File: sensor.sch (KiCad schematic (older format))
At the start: 67 parts, among them CON1 Micro USB, CON2 PROG, CON3 N.C., CON4 HTU21D, CON5 PMS3003/5003, CON6 AUX, Q1 BSS214N, Q2 BSS214N, Q3 BSS214N, SW1 RESET, SW2 CFG, U1 N.C., U2 TLV1117LV33DCY, U3 ESP-12F, U4 HTU21D, U5 PMS7003

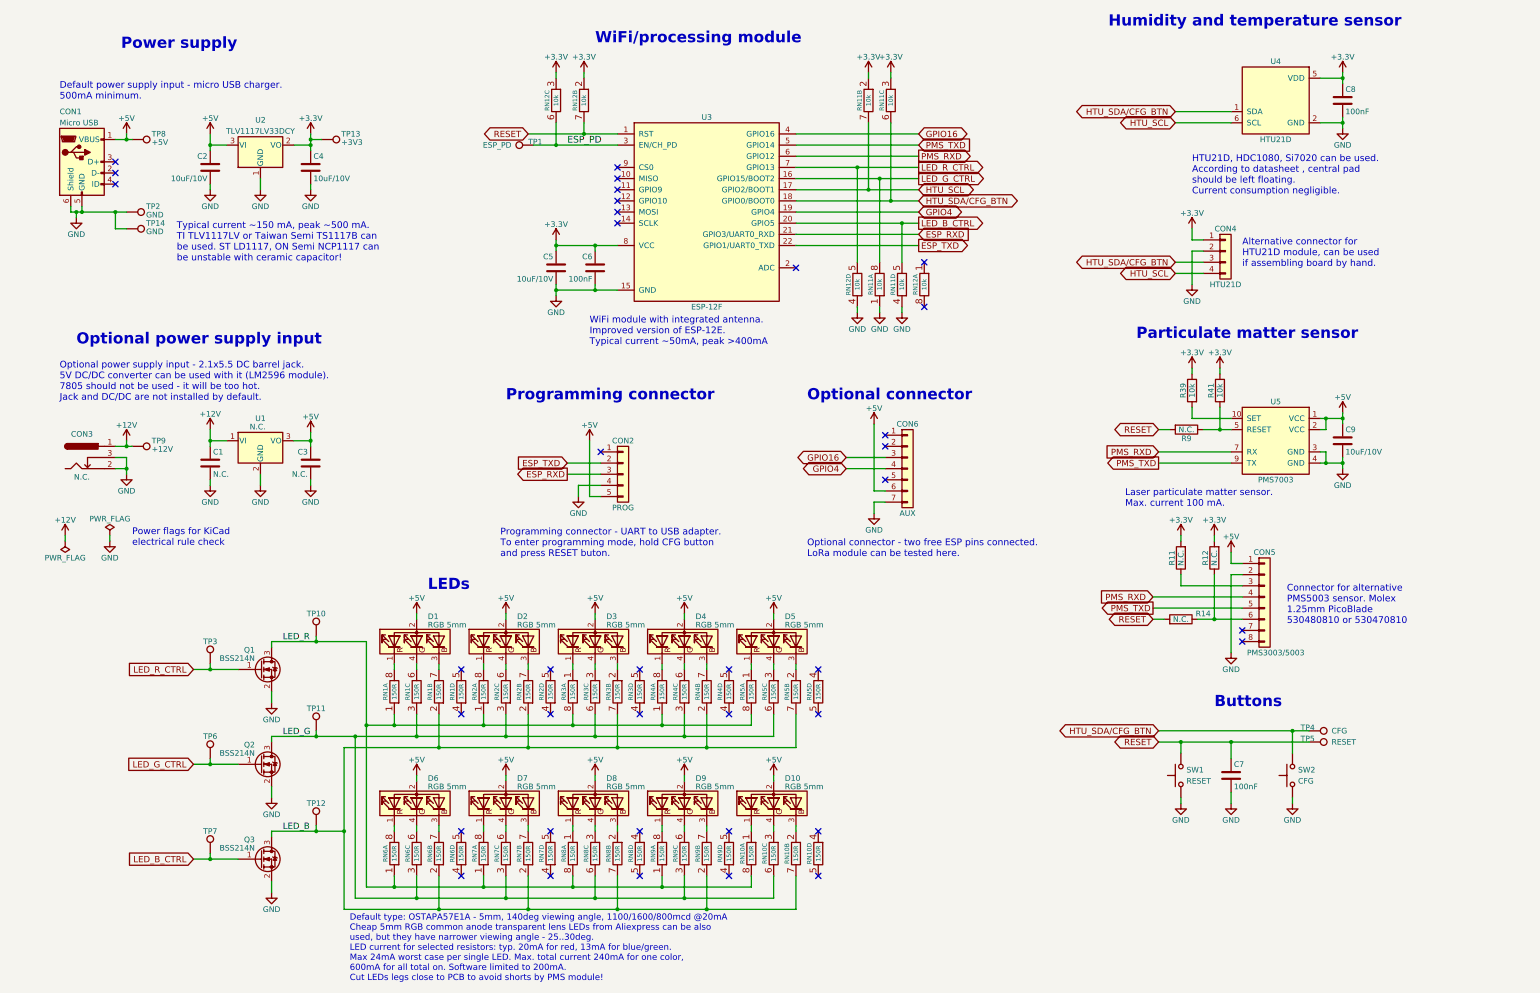
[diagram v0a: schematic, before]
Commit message: Add connector for SDS011 Close #10
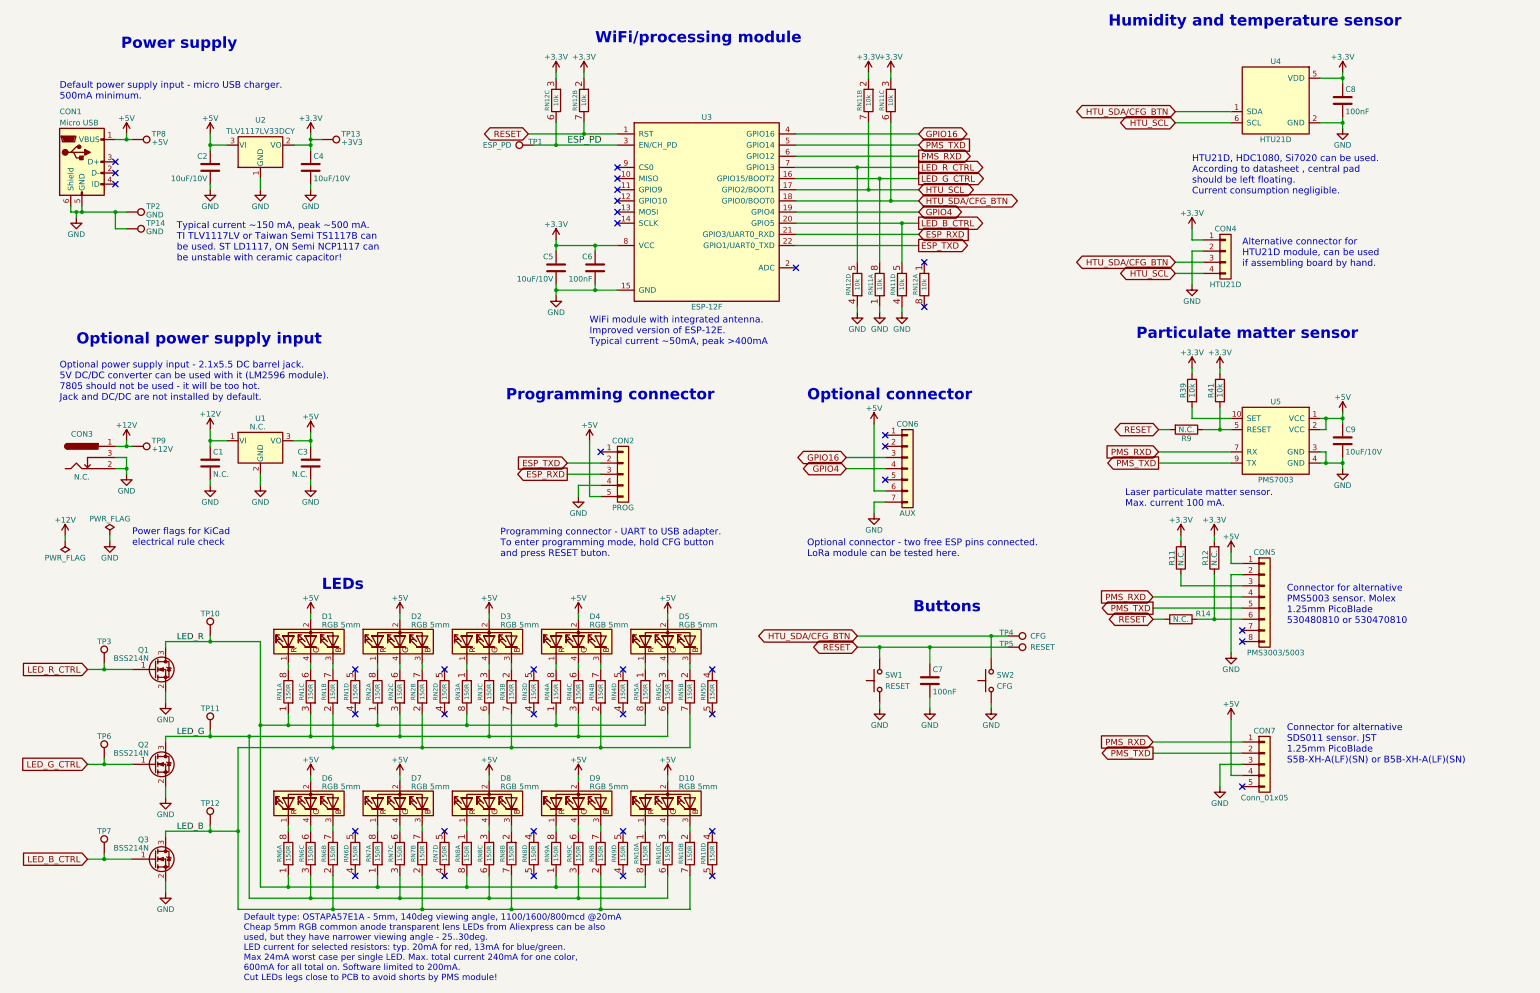
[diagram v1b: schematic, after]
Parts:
- added CON7: Conn_01x05, less-smog:B5B-XH-A(LF)(SN), symbol Conn_01x05
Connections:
- net +5V: now also CON7.4 (Pin_4)
- net GND: now also CON7.3 (Pin_3)
- net PMS_RXD: now also CON7.1 (Pin_1)
- net PMS_TXD: now also CON7.2 (Pin_2)
- no-connect marks 38 -> 39
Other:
- note added: "Connector for alternative\nSDS011 sensor. JST\n1.25mm PicoBlade\nS5B-XH-A(LF)(SN) or B5B-XH-A(LF)(SN)"
- moved on the sheet: C7, D1, D10, D2, D3, D4, D5, D6, D7, D8, D9, Q1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

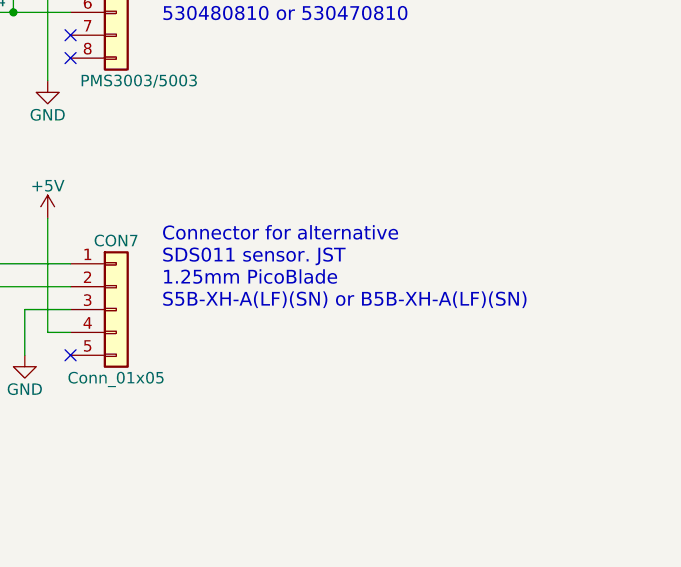
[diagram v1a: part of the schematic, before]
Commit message: [#10] Update schematic PDF. Add remaining library footprints.
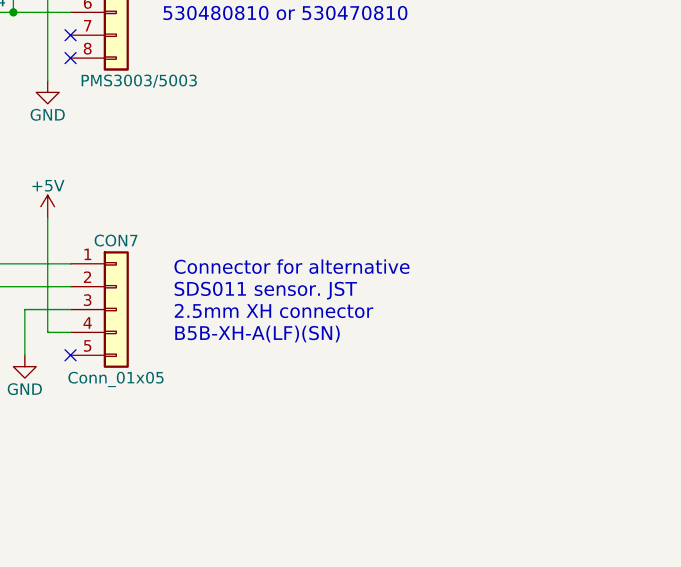
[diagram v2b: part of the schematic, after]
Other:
- note added: "Connector for alternative\nSDS011 sensor. JST\n2.5mm XH connector\nB5B-XH-A(LF)(SN)"
- note removed: "Connector for alternative\nSDS011 sensor. JST\n1.25mm PicoBlade\nS5B-XH-A(LF)(SN) or B5B-XH-A(LF)(SN)"

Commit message: Update silkscreen
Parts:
- CON7: value Conn_01x05 -> SDS011
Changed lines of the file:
@@
 P 11800 7350
 F 0 "CON7" H 11800 7650 50  0000 C CNN
-F 1 "Conn_01x05" H 11800 7050 50  0000 C CNN
+F 1 "SDS011" H 11800 7050 50  0000 C CNN
 F 2 "less-smog:B5B-XH-A(LF)(SN)" H 11800 7350 50  0001 C CNN
 F 3 "" H 11800 7350 50  0001 C CNN
